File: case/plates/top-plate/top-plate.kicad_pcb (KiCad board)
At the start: 2 copper layers, 140.5 x 112.5 mm, 0 parts

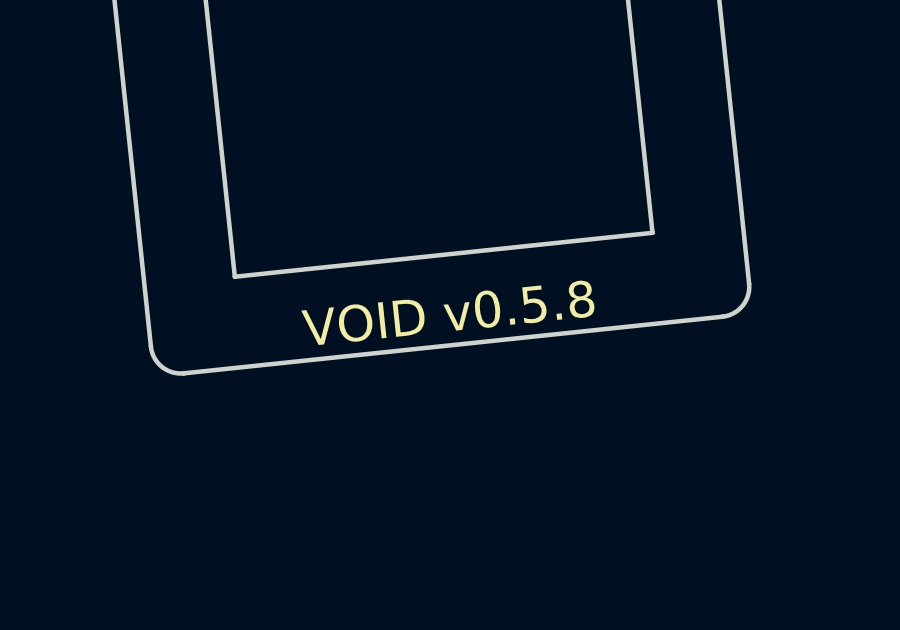
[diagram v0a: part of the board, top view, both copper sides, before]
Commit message: Mcu cover (#7)
* more plates

* updated workflow

* mcu cover

* small change
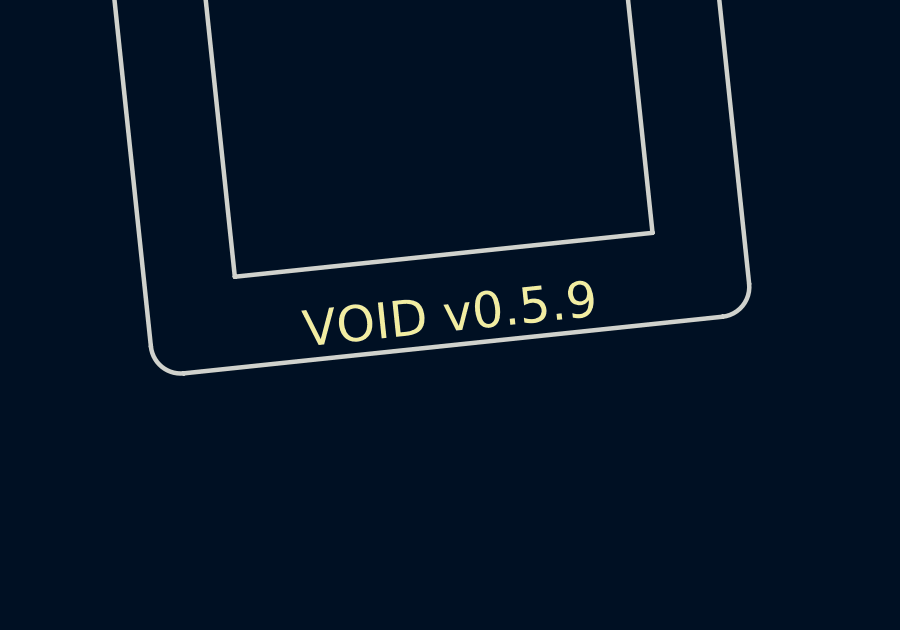
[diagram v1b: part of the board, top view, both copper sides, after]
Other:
- board text added: "VOID v0.5.9"
- board text removed: "VOID v0.5.8"
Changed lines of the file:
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@@
 	(paper "A4")
 	(title_block
-		(title "top_plate")
-		(date "2024-11-10")
-		(rev "0.5.8")
+		(title "VOID Top Plate")
+		(date "2024-11-17")
+		(rev "0.5.9")
 		(company "Allen Choi")
 	)
@@
 		)
 	)
-	(gr_text "VOID v0.5.8"
+	(gr_text "VOID v0.5.9"
 		(at 113.174903 120.310023 6)
 		(layer "B.SilkS")
 		(effects
 			(font
-				(face "Android Robot")
+				(face "ANDROID ROBOT")
 				(size 1.2 1.2)
 				(thickness 0.15)
@@
 			(justify mirror)
 		)
-		(render_cache "VOID v0.5.8" 6
+		(render_cache "VOID v0.5.9" 6
 			(polygon
 				(pts
@@
 			(polygon
 				(pts
-					(xy 109.397208 120.09825) (xy 109.418714 120.105061) (xy 109.470534 120.137365) (xy 109.495974 120.193963)
-					(xy 109.51696 120.393631) (xy 109.515751 120.415809) (xy 109.488674 120.469396) (xy 109.472491 120.482766)
-					(xy 109.425469 120.518141) (xy 109.373137 120.555967) (xy 109.318354 120.594884) (xy 109.267214 120.630858)
-					(xy 109.209573 120.671134) (xy 109.20991 120.67434) (xy 109.454352 120.787749) (xy 109.497652 120.808005)
-					(xy 109.536351 120.85333) (xy 109.552715 120.913271) (xy 109.570607 121.083498) (xy 109.560878 121.12586)
-					(xy 109.528701 121.176487) (xy 109.471746 121.199983) (xy 108.609822 121.290575) (xy 108.580336 121.290432)
-					(xy 108.546917 121.276192) (xy 108.504026 121.234262) (xy 108.486559 121.177691) (xy 108.472507 121.043999)
-					(xy 108.718292 121.043999) (xy 109.314089 120.981378) (xy 109.000463 120.832213) (xy 108.994051 120.832887)
-					(xy 108.718292 121.043999) (xy 108.472507 121.043999) (xy 108.469678 121.017082) (xy 108.468712 120.997429)
-					(xy 108.48451 120.939489) (xy 108.506685 120.912803) (xy 108.553302 120.873391) (xy 108.602334 120.835246)
-					(xy 108.651 120.798734) (xy 108.708058 120.756891) (xy 108.756358 120.722011) (xy 108.756021 120.718804)
-					(xy 108.709988 120.698453) (xy 108.652497 120.672423) (xy 108.595672 120.642825) (xy 108.55531 120.627479)
-					(xy 108.497014 120.599724) (xy 108.445134 120.562361) (xy 108.41634 120.509605) (xy 108.405829 120.409602)
-					(xy 108.641594 120.409602) (xy 108.968673 120.560594) (xy 109.257212 120.344897) (xy 108.641594 120.409602)
-					(xy 108.405829 120.409602) (xy 108.393608 120.293323) (xy 108.401865 120.265711) (xy 108.435065 120.213902)
-					(xy 108.489767 120.190384) (xy 109.368888 120.097985)
+					(xy 109.362184 120.098689) (xy 108.483354 120.191058) (xy 108.427942 120.214651) (xy 108.394184 120.266519)
+					(xy 108.385738 120.29415) (xy 108.387116 120.307267) (xy 108.480067 121.191635) (xy 108.506814 121.248191)
+					(xy 108.553176 121.285535) (xy 108.603701 121.291218) (xy 109.491858 121.197869) (xy 109.547923 121.174208)
+					(xy 109.582089 121.122297) (xy 109.59064 121.094654) (xy 109.557308 120.777518) (xy 109.550604 120.778222)
+					(xy 109.325577 120.801874) (xy 109.326281 120.808578) (xy 109.344112 120.978223) (xy 108.699054 121.046021)
+					(xy 108.638455 120.469462) (xy 108.632266 120.410582) (xy 109.251091 120.345541) (xy 108.942069 120.576652)
+					(xy 108.857247 120.585567) (xy 108.857951 120.592271) (xy 108.881695 120.818173) (xy 108.888107 120.817499)
+					(xy 108.979634 120.807879) (xy 109.039405 120.790216) (xy 109.092341 120.757242) (xy 109.132199 120.722883)
+					(xy 109.190116 120.681379) (xy 109.242876 120.643297) (xy 109.290478 120.608638) (xy 109.345926 120.56775)
+					(xy 109.402341 120.525195) (xy 109.451129 120.486678) (xy 109.484089 120.456616) (xy 109.504612 120.398868)
+					(xy 109.504353 120.369022) (xy 109.487657 120.210162) (xy 109.470045 120.154186) (xy 109.426515 120.112765)
+					(xy 109.392544 120.09874)
 				)
 			)
@@
 		)
 	)
-	(gr_text "VOID v0.5.8"
+	(gr_text "VOID v0.5.9"
 		(at 113.174903 120.310023 6)
 		(layer "F.SilkS")
 		(effects
 			(font
-				(face "Android Robot")
+				(face "ANDROID ROBOT")
 				(size 1.2 1.2)
 				(thickness 0.15)
 			)
 		)
-		(render_cache "VOID v0.5.8" 6
+		(render_cache "VOID v0.5.9" 6
 			(polygon
 				(pts
@@
 			(polygon
 				(pts
-					(xy 117.791179 119.230535) (xy 117.834425 119.274309) (xy 117.848242 119.299601) (xy 117.870975 119.515883)
-					(xy 117.853778 119.573473) (xy 117.810801 119.620806) (xy 117.759549 119.660074) (xy 117.723259 119.683477)
-					(xy 117.67383 119.724243) (xy 117.623007 119.761657) (xy 117.582212 119.791134) (xy 117.582549 119.79434)
-					(xy 117.637045 119.818416) (xy 117.701556 119.847482) (xy 117.75675 119.873078) (xy 117.812641 119.900196)
-					(xy 117.866434 119.929054) (xy 117.893672 119.950546) (xy 117.921171 120.003935) (xy 117.924313 120.02336)
-					(xy 117.941193 120.183969) (xy 117.93587 120.242935) (xy 117.902634 120.292867) (xy 117.872905 120.313744)
-					(xy 117.844093 120.320014) (xy 116.98217 120.410606) (xy 116.921574 120.399465) (xy 116.879574 120.356634)
-					(xy 116.86125 120.317221) (xy 116.845146 120.163999) (xy 117.090931 120.163999) (xy 117.686728 120.101378)
-					(xy 117.373102 119.952214) (xy 117.36669 119.952888) (xy 117.090931 120.163999) (xy 116.845146 120.163999)
-					(xy 116.843359 120.146993) (xy 116.846903 120.084961) (xy 116.875332 120.032579) (xy 116.913475 120.003764)
-					(xy 117.128997 119.842011) (xy 117.12866 119.838804) (xy 117.063904 119.811392) (xy 117.006402 119.786837)
-					(xy 116.944725 119.760161) (xy 116.885672 119.734042) (xy 116.832323 119.709216) (xy 116.813713 119.699504)
-					(xy 116.776087 119.652717) (xy 116.770293 119.631275) (xy 116.759607 119.529602) (xy 117.014233 119.529602)
-					(xy 117.341312 119.680594) (xy 117.629851 119.464898) (xy 117.014233 119.529602) (xy 116.759607 119.529602)
-					(xy 116.749308 119.431607) (xy 116.762424 119.370956) (xy 116.806395 119.328584) (xy 116.826016 119.317451)
-					(xy 116.853661 119.311303) (xy 117.732783 119.218904)
-				)
-			)
+					(xy 116.860365 119.310599) (xy 117.739195 119.21823) (xy 117.798301 119.229786) (xy 117.842106 119.273502)
+					(xy 117.856112 119.298774) (xy 117.857491 119.311891) (xy 117.950442 120.196259) (xy 117.936039 120.25714)
+					(xy 117.898453 120.303307) (xy 117.850214 120.319371) (xy 116.962057 120.41272) (xy 116.902298 120.401232)
+					(xy 116.858086 120.357559) (xy 116.843974 120.332298) (xy 116.810642 120.015162) (xy 116.817346 120.014457)
+					(xy 117.042373 119.990806) (xy 117.043077 119.99751) (xy 117.060908 120.167155) (xy 117.705966 120.099356)
+					(xy 117.645367 119.522797) (xy 117.639179 119.463917) (xy 117.020354 119.528958) (xy 117.370674 119.69077)
+					(xy 117.455496 119.681855) (xy 117.456201 119.688559) (xy 117.479944 119.914461) (xy 117.473531 119.915135)
+					(xy 117.382005 119.924754) (xy 117.319867 119.919904) (xy 117.261232 119.898657) (xy 117.215101 119.873335)
+					(xy 117.149821 119.84478) (xy 117.090296 119.8185) (xy 117.036528 119.794496) (xy 116.973792 119.766029)
+					(xy 116.909761 119.736133) (xy 116.854031 119.708601) (xy 116.815541 119.68605) (xy 116.78346 119.63383)
+					(xy 116.777508 119.604583) (xy 116.760811 119.445723) (xy 116.7664 119.387309) (xy 116.800366 119.337742)
+					(xy 116.830679 119.31696)
+				)
+			)

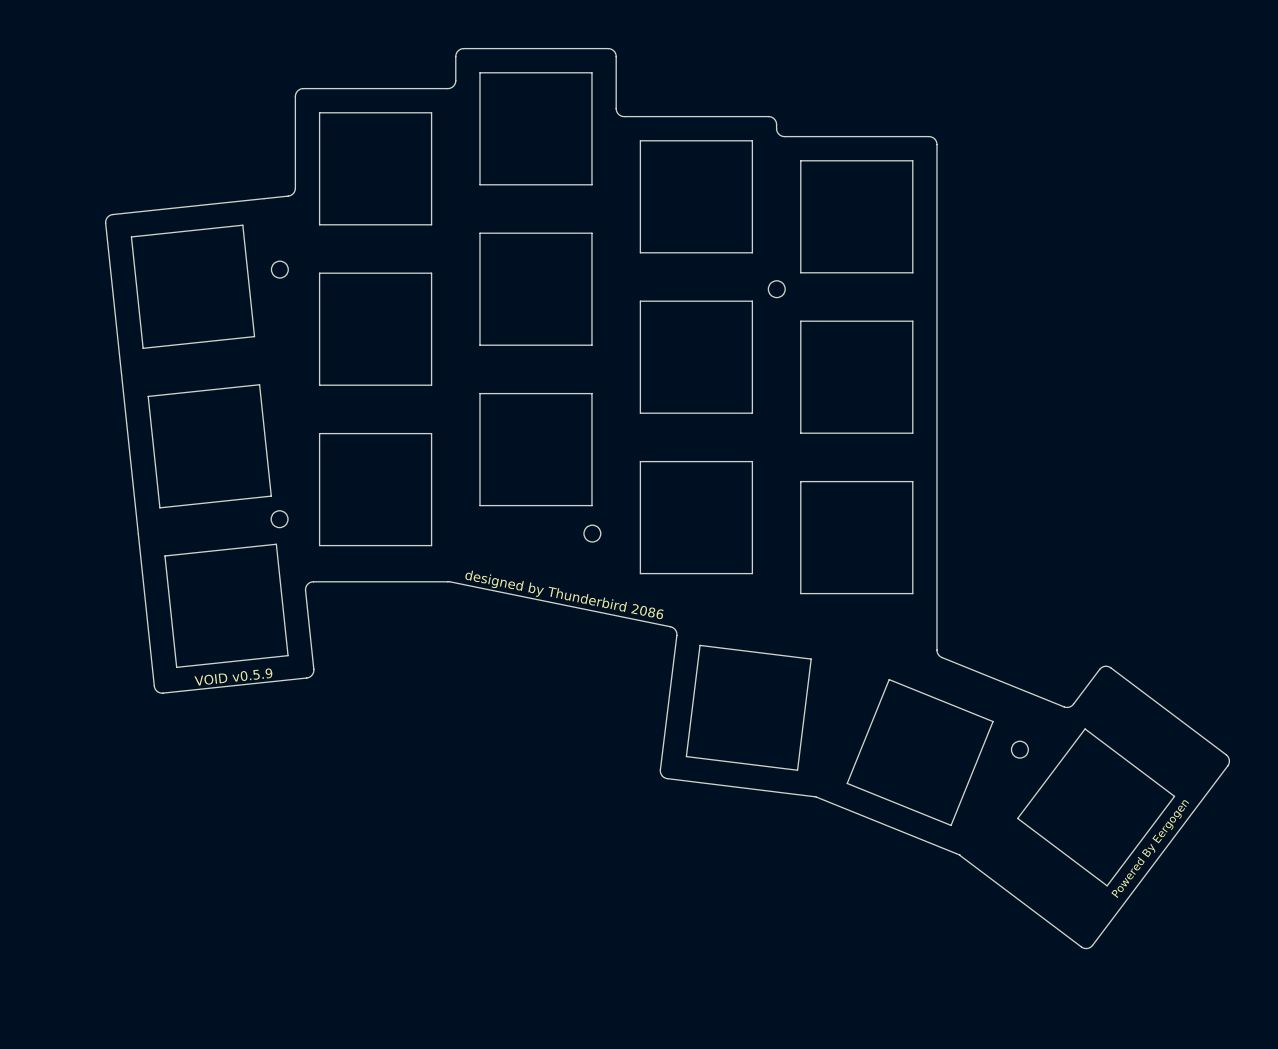
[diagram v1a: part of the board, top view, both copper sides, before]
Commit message: Changed TRRS to USB-C connector (#14)
* usb-c mod for hybrid

* updated
  - submodule
  - ergogen yaml
  - schematic and pcb

* updated cherry-mx

usb-c for communication between left and right hand sides

* updated choc

* updated choc

* fixed corner

* void-choc

* ergogen
  - bottom plate
  - charger plate

* updated choc

* updated ergogen

* cherry-mx
* hybrid-mx

* updated ergogen for VOID Choc

* refreshed submodule

* updated ergogen yaml

* updated PCBs

* updated version
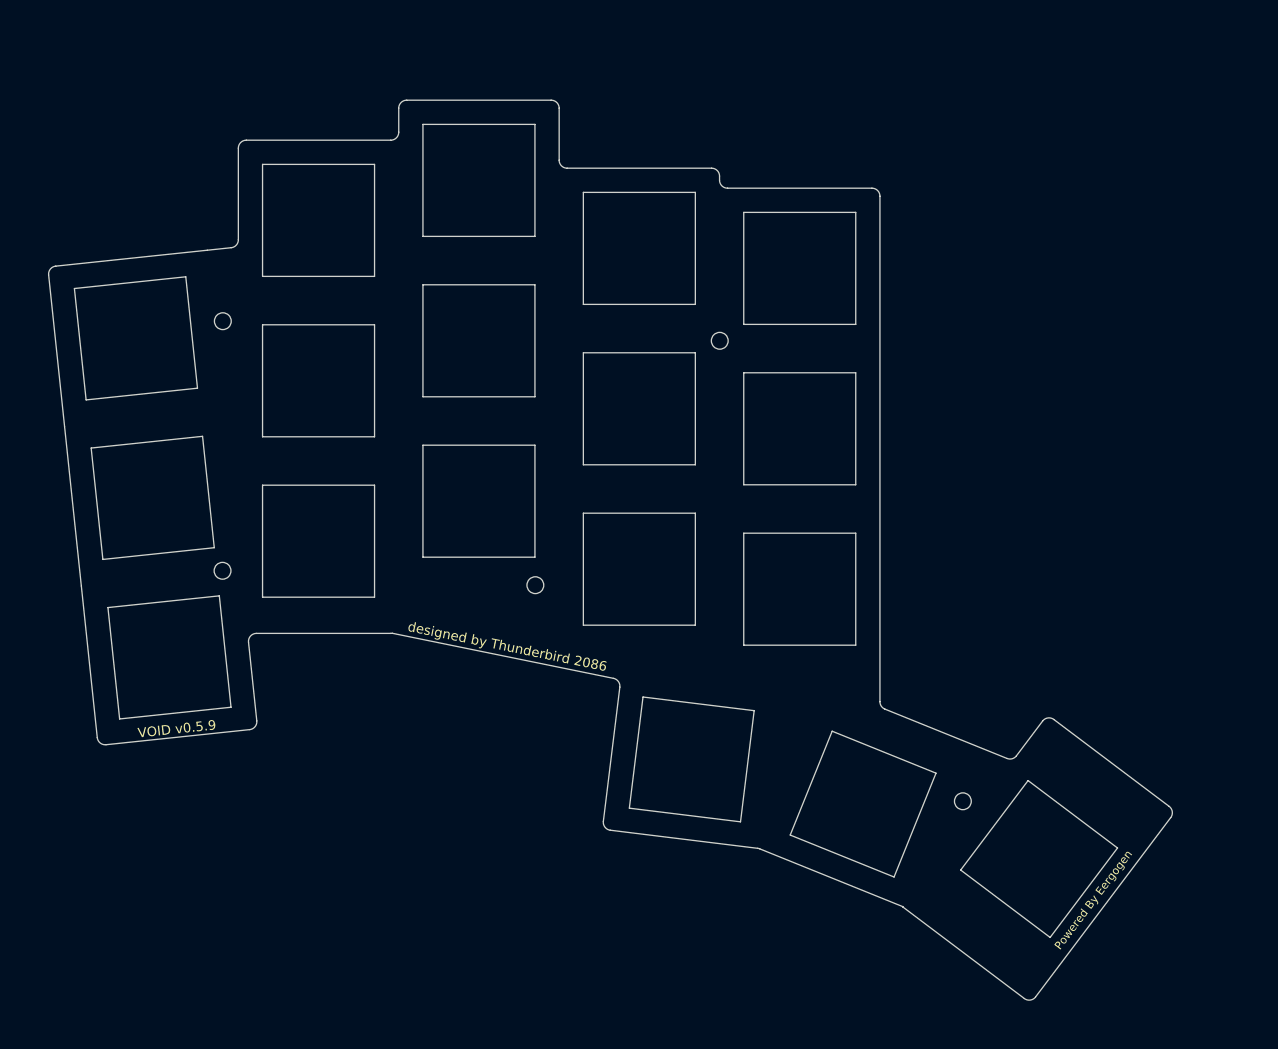
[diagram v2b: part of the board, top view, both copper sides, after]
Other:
- board text added: "offset: 90, 70 from origin"
